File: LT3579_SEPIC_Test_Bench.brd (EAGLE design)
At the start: 64.4 x 62.2 mm, 164 parts

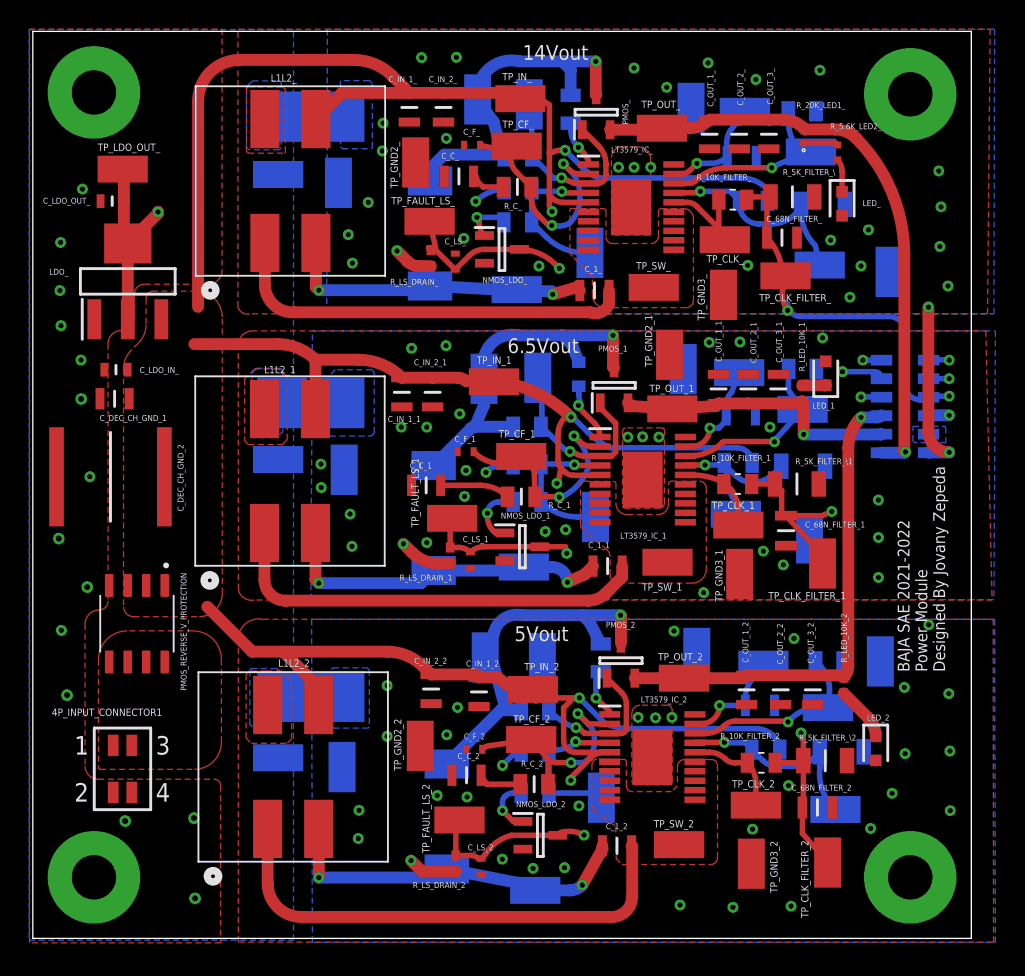
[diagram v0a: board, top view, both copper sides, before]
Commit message: Modified Board Layout
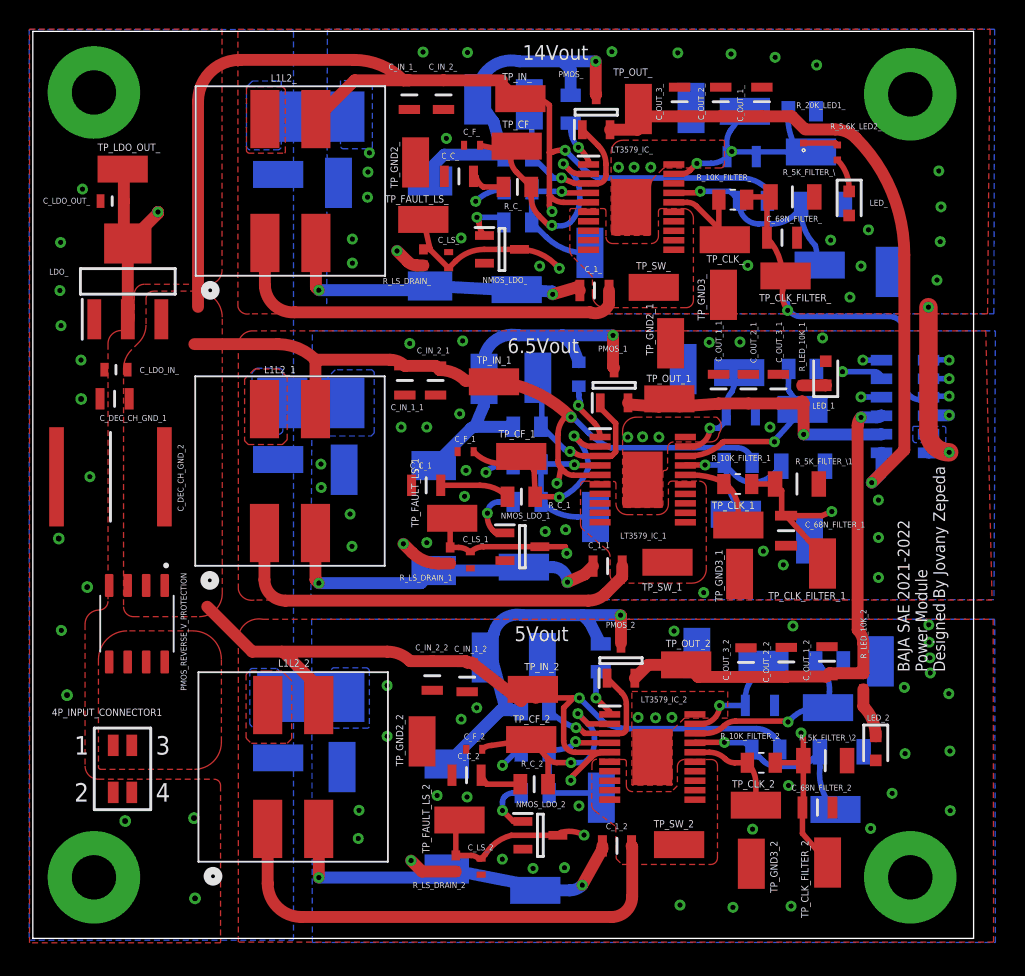
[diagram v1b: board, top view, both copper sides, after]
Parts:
- moved C_OUT_3_ 6.52 mm to (44.4, 57.4), turned to 90 degrees
- moved C_OUT_1_2 5.85 mm to (54.5, 19.0), turned to 90 degrees
- moved C_OUT_3_2 4.96 mm to (48.9, 18.9), turned to 90 degrees
- moved C_OUT_1_ 4.23 mm to (50.0, 57.4), turned to 90 degrees
- moved C_OUT_2_ 2.56 mm to (47.2, 57.4), turned to 90 degrees
- moved TP_OUT_ 2.08 mm to (41.5, 56.9), turned to 270 degrees
- moved C_OUT_2_2 1.95 mm to (51.7, 19.0), turned to 90 degrees
- moved R_LED_10K_2 1.37 mm to (57.0, 17.6)
- moved C_IN_1_2 1.30 mm to (29.8, 17.9)
- moved TP_OUT_2 0.93 mm to (44.8, 18.8)
- moved C_IN_2_2 0.92 mm to (27.4, 18.0)
- moved C_IN_1_ 0.86 mm to (25.8, 57.9)
- moved C_IN_2_ 0.86 mm to (28.2, 57.9)
- moved C_IN_2_1 0.84 mm to (27.6, 38.3)
- moved C_IN_1_1 0.84 mm to (25.5, 38.3)
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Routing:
- net VOUT_: track 41.2 -> 46.4 mm
- net RT_: track 13.7 -> 9.29 mm
- net GND_2: track 16.4 -> 18.7 mm, vias 31 -> 34
- net VOUT_2: track 34.0 -> 35.8 mm
- net LDO_OUT_: track 92.4 -> 91.9 mm
- net VIN: track 207.5 -> 208.0 mm
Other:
- board size 64.4 x 62.2 mm -> 64.5 x 62.2 mm

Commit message: Added more GND Vias, Changes text size, moved texts, clears DRC error
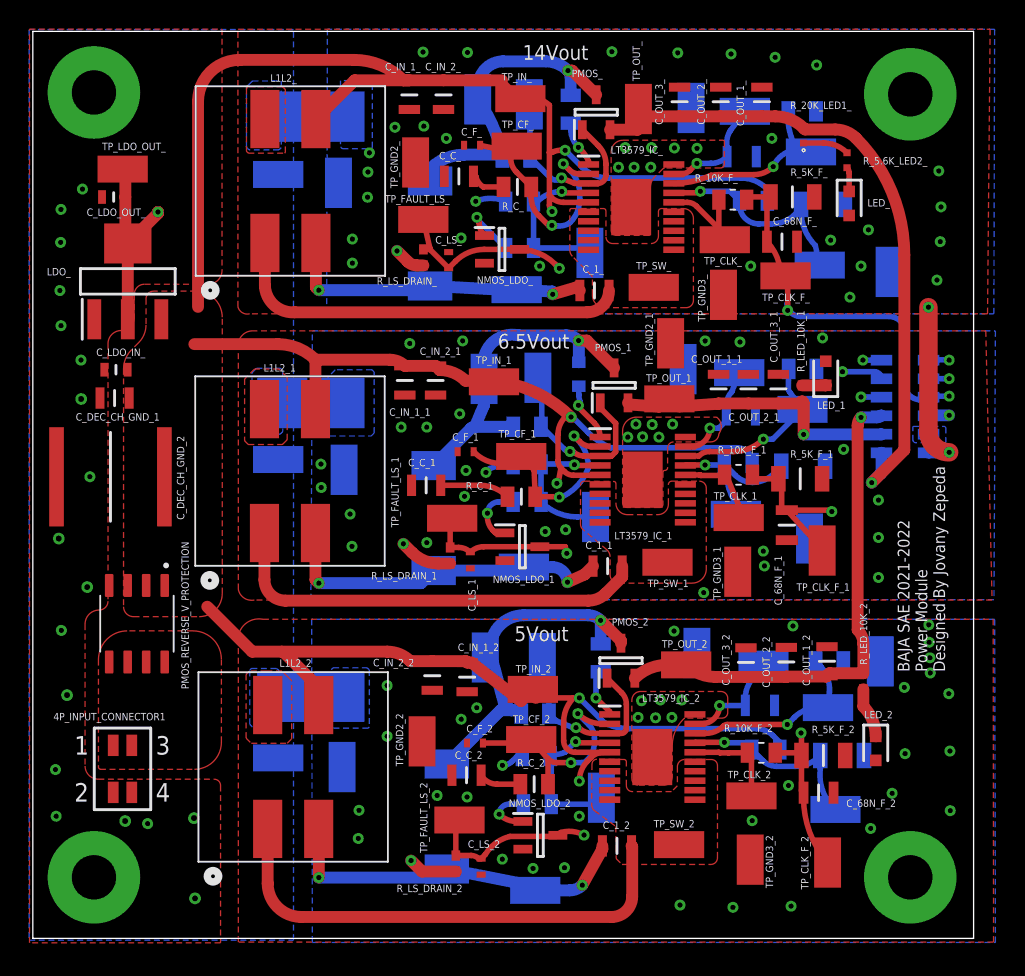
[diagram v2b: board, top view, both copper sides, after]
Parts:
- removed C_68N_FILTER_, C_68N_FILTER_1, C_68N_FILTER_2: CEU4J2X7R1H683K125AE, SamacSys_Parts:CAPC2013X150N
- removed R_10K_FILTER_1, R_10K_FILTER_2: AC0805DR-0710KL, AC0805DR-0710KL:RESC2012X60N
- removed R_5K_FILTER_\1, R_5K_FILTER_\2: RT1206BRD075KL, SamacSys_Parts:RESC3116X65N
- removed TP_CLK_FILTER_1: S1751-46R, S1751-46R:S1751-46R_
- added C_68N_F_, C_68N_F_1, C_68N_F_2: CEU4J2X7R1H683K125AE, SamacSys_Parts:CAPC2013X150N
- added R_10K_F_1, R_10K_F_2: AC0805DR-0710KL, AC0805DR-0710KL:RESC2012X60N
- added R_5K_F_1, R_5K_F_2: RT1206BRD075KL, SamacSys_Parts:RESC3116X65N
- added TP_CLK_F_1: S1751-46R, S1751-46R:S1751-46R_
- moved R_LS_GATE_ 1.76 mm to (33.4, 47.4)
- moved R_5.6K_LED2_ 0.85 mm to (55.9, 53.4)
- moved R_FAULT_ 0.84 mm to (33.4, 50.5)
- moved R_LS_GATE_2 0.78 mm to (34.6, 9.21)
- moved TP_CLK_2 0.70 mm to (49.3, 9.78)
- moved TP_CLK_1 0.51 mm to (48.4, 28.9)
- moved C_F_2 0.43 mm to (30.3, 13.4)
- moved R_FAULT_2 0.31 mm to (34.5, 12.5)
- moved C_LDO_OUT_ 0.30 mm to (5.55, 50.9)
- moved TP_GND3_2 0.29 mm to (49.2, 5.40)
- moved R_UVLO2_2 0.26 mm to (55.5, 12.5)
- moved R_GATE_2 0.23 mm to (34.5, 15.4)
- moved TP_GND3_1 0.20 mm to (48.4, 25.2)
- moved R_GATE_ 0.15 mm to (33.2, 53.6)
- moved C_DEC_CH_GND_1 0.05 mm to (5.61, 37.1)
- renumbered R_10K_FILTER_ to R_10K_F_, R_5K_FILTER_\ to R_5K_F_, TP_CLK_FILTER_ to TP_CLK_F_, TP_CLK_FILTER_2 to TP_CLK_F_2
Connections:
- net CLK_1: now also R_10K_F_1.1; no longer R_10K_FILTER_1.1
- net CLK_2: now also R_10K_F_2.1; no longer R_10K_FILTER_2.1
- net CLK_FILTER_OUT_: now also C_68N_F_.1; no longer C_68N_FILTER_.1
- net CLK_FILTER_OUT_1: now also C_68N_F_1.1, R_10K_F_1.2, R_5K_F_1.1, TP_CLK_F_1.1; no longer C_68N_FILTER_1.1, R_10K_FILTER_1.2, R_5K_FILTER_\1.1, TP_CLK_FILTER_1.1
- net CLK_FILTER_OUT_2: now also C_68N_F_2.1, R_10K_F_2.2, R_5K_F_2.1; no longer C_68N_FILTER_2.1, R_10K_FILTER_2.2, R_5K_FILTER_\2.1
- net GND_: now also C_68N_F_.2; no longer C_68N_FILTER_.2
- net GND_1: now also C_68N_F_1.2, R_5K_F_1.2; no longer C_68N_FILTER_1.2, R_5K_FILTER_\1.2
- net GND_2: now also C_68N_F_2.2, R_5K_F_2.2; no longer C_68N_FILTER_2.2, R_5K_FILTER_\2.2
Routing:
- net RT_: track 9.29 -> 13.8 mm
- net N$13: track 24.9 -> 22.7 mm
- net N$3: track 25.2 -> 23.1 mm
- net N$7: track 26.0 -> 24.3 mm
- net N$8: track 3.35 -> 4.27 mm
- net N$12: track 2.37 -> 3.11 mm
- net N$15: track 2.32 -> 1.66 mm
- net VOUT_2: track 35.8 -> 35.2 mm
- net GND_2: vias 34 -> 37
- net GND_: vias 29 -> 36

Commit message: Used SRC to change the LBR reference of each componant
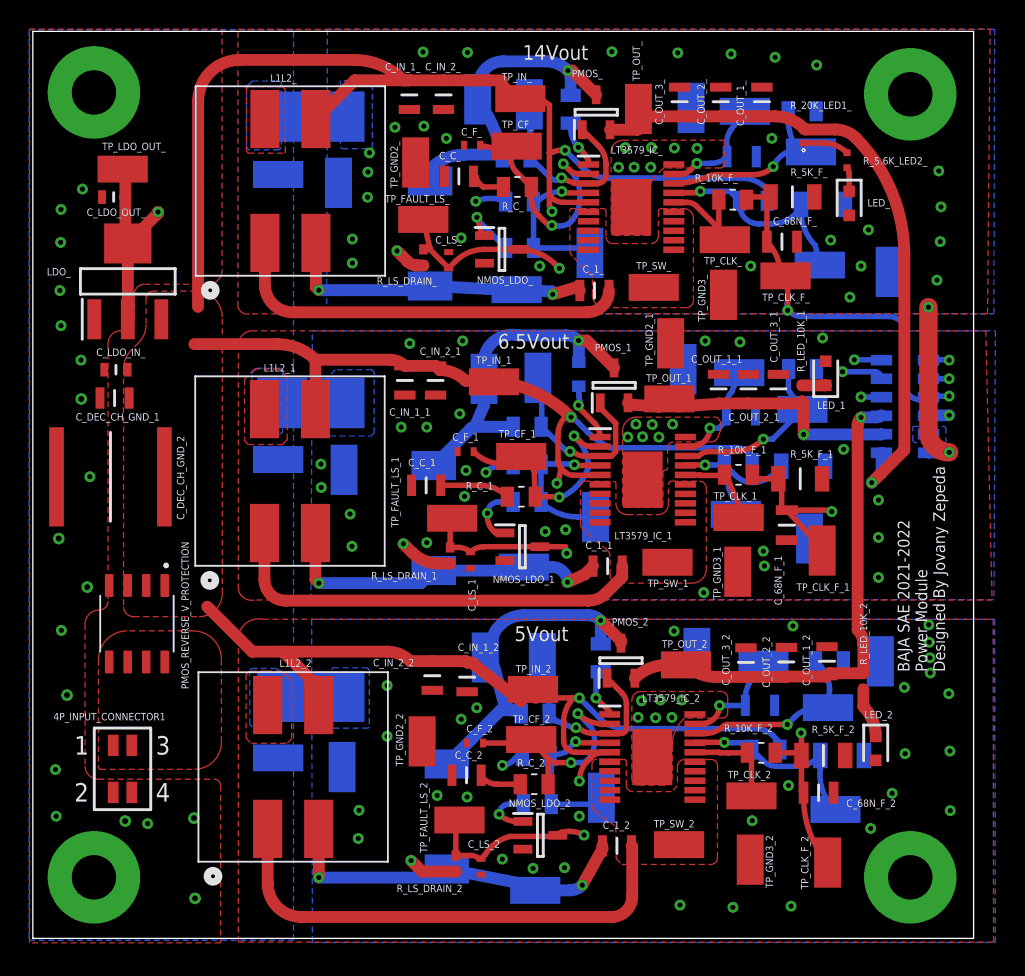
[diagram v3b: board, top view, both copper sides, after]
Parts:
- 12P_OUTPUT_CONNECTOR1: device SamacSys_Parts:CLP-106-02-XXX -> LT3579_SEPIC_Test_Bench:CLP-106-02-XXX
- 4P_INPUT_CONNECTOR1: device SAMTEC-CLP-102-02-X-D:SAMTEC-CLP-102-02-X-D -> LT3579_SEPIC_Test_Bench:SAMTEC-CLP-102-02-X-D
- C_1_, C_1_1, C_1_2, C_IN_1_, C_IN_1_1, C_IN_1_2, C_IN_2_, C_IN_2_1, C_IN_2_2, C_OUT_1_, C_OUT_1_1, C_OUT_1_2, C_OUT_2_, C_OUT_2_1, C_OUT_2_2, C_OUT_3_, C_OUT_3_1, C_OUT_3_2, C_SS_, C_SS_1, C_SS_2: device SamacSys_Parts:CAPC2012X145N -> LT3579_SEPIC_Test_Bench:CAPC2012X145N
- C_68N_F_, C_68N_F_1, C_68N_F_2: device SamacSys_Parts:CAPC2013X150N -> LT3579_SEPIC_Test_Bench:CAPC2013X150N
- C_C_, C_C_1, C_C_2, C_DEC_CH_GND_1: device SamacSys_Parts:CAPC2012X100N -> LT3579_SEPIC_Test_Bench:CAPC2012X100N
- C_DEC_CH_GND_2: device SamacSys_Parts:CAPC7563X250N -> LT3579_SEPIC_Test_Bench:CAPC7563X250N
- C_F_, C_F_1, C_F_2, C_LS_, C_LS_1, C_LS_2: device SamacSys_Parts:CAPC1005X55N -> LT3579_SEPIC_Test_Bench:CAPC1005X55N
- C_LDO_IN_, C_LDO_OUT_: device SamacSys_Parts:CAPC1608X90N -> LT3579_SEPIC_Test_Bench:CAPC1608X90N
- D1_, D1_1, D1_2: device SamacSys_Parts:DIOM7958X256N -> LT3579_SEPIC_Test_Bench:DIOM7958X256N
- L1L2_, L1L2_1, L1L2_2: device MSD1278T-Series:MSD1278T-822MLXX -> LT3579_SEPIC_Test_Bench:MSD1278T-822MLXX
- LDO_: device SamacSys_Parts:SOT230P700X180-4N -> LT3579_SEPIC_Test_Bench:SOT230P700X180-4N
- LED_, LED_1, LED_2: device SamacSys_Parts:APT1608CGCK -> LT3579_SEPIC_Test_Bench:APT1608CGCK
- LT3579_IC_, LT3579_IC_1, LT3579_IC_2: device SamacSys_Parts:SOP65P640X120-21N -> LT3579_SEPIC_Test_Bench:SOP65P640X120-21N
- NMOS_LDO_, NMOS_LDO_1, NMOS_LDO_2, PMOS_, PMOS_1, PMOS_2: device SamacSys_Parts:SOT95P280X100-3N -> LT3579_SEPIC_Test_Bench:SOT95P280X100-3N
- PMOS_REVERSE_V_PROTECTION: device DMP3015LSSQ-13:SOIC127P600X170-8N -> LT3579_SEPIC_Test_Bench:SOIC127P600X170-8N
- R_10K_F_, R_10K_F_1, R_10K_F_2: device AC0805DR-0710KL:RESC2012X60N -> LT3579_SEPIC_Test_Bench:RESC2012X60N
- R_20K_LED1_: device SamacSys_Parts:ERJ2R_(0402) -> LT3579_SEPIC_Test_Bench:ERJ2R_(0402)
- R_5.6K_LED2_: device SamacSys_Parts:ERA2AED122X -> LT3579_SEPIC_Test_Bench:ERA2AED122X
- R_5K_F_, R_5K_F_1, R_5K_F_2, R_UVLO2_, R_UVLO2_1, R_UVLO2_2: device SamacSys_Parts:RESC3116X65N -> LT3579_SEPIC_Test_Bench:RESC3116X65N
- R_C_, R_C_1, R_C_2, R_GATE_, R_GATE_1, R_GATE_2, R_T_, R_T_1, R_T_2: device SamacSys_Parts:RESC2012X60N -> LT3579_SEPIC_Test_Bench:RESC2012X60N
- R_FAULT_, R_FAULT_1, R_FAULT_2, R_LS_GATE_, R_LS_GATE_1, R_LS_GATE_2: device AT0805FRE07100KL:RESC2012X60N -> LT3579_SEPIC_Test_Bench:RESC2012X60N
- R_FB_: device AC0805FR-07150KL:RESC2012X60N -> LT3579_SEPIC_Test_Bench:RESC2012X60N
- R_FB_1: device AC0603FR-0764K9L:RESC1608X55N -> LT3579_SEPIC_Test_Bench:RESC1608X55N
- R_FB_2: device AC0805FR-0745K3L:RESC2012X60N -> LT3579_SEPIC_Test_Bench:RESC2012X60N
- R_LED_10K_1, R_LED_10K_2, R_LS_DRAIN_, R_LS_DRAIN_1, R_LS_DRAIN_2: device SamacSys_Parts:RESC1005X37N -> LT3579_SEPIC_Test_Bench:RESC1005X37N
- R_SHUNT_GND_, R_SHUNT_GND_1, R_SHUNT_GND_2: device GMR100HTCFAR100:RESC6432X55N -> LT3579_SEPIC_Test_Bench:RESC6432X55N
- R_UVLO1_, R_UVLO1_1, R_UVLO1_2: device AC0805FR-0730KL:RESC2012X60N -> LT3579_SEPIC_Test_Bench:RESC2012X60N
- TP_CF_, TP_CF_1, TP_CF_2, TP_CH_GND_, TP_CH_GND_1, TP_CH_GND_2, TP_CLK_, TP_CLK_1, TP_CLK_2, TP_CLK_F_, TP_CLK_F_1, TP_CLK_F_2, TP_D1_, TP_D1_1, TP_D1_2, TP_FAULT_, TP_FAULT_1, TP_FAULT_2, TP_FAULT_LS_, TP_FAULT_LS_1, TP_FAULT_LS_2, TP_FB_, TP_FB_1, TP_FB_2, TP_GATE_, TP_GATE_1, TP_GATE_2, TP_GND1_, TP_GND1_1, TP_GND1_2, TP_GND2_, TP_GND2_1, TP_GND2_2, TP_GND3_, TP_GND3_1, TP_GND3_2, TP_GND4_, TP_GND4_1, TP_GND4_2, TP_GND_, TP_GND_1, TP_GND_2, TP_IN_, TP_IN_1, TP_IN_2, TP_LDO_OUT_, TP_OUT_, TP_OUT_1, TP_OUT_2, TP_RT_, TP_RT_1, TP_RT_2, TP_SHDN_, TP_SHDN_1, TP_SHDN_2, TP_SS_, TP_SS_1, TP_SS_2, TP_SW_, TP_SW_1, TP_SW_2: device S1751-46R:S1751-46R_ -> LT3579_SEPIC_Test_Bench:S1751-46R_
- U$1, U$2, U$3, U$4: device THROUGH_HOLE:THROUGH_HOLE -> LT3579_SEPIC_Test_Bench:THROUGH_HOLE

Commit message: Modifed board. Connected GND planes Together.
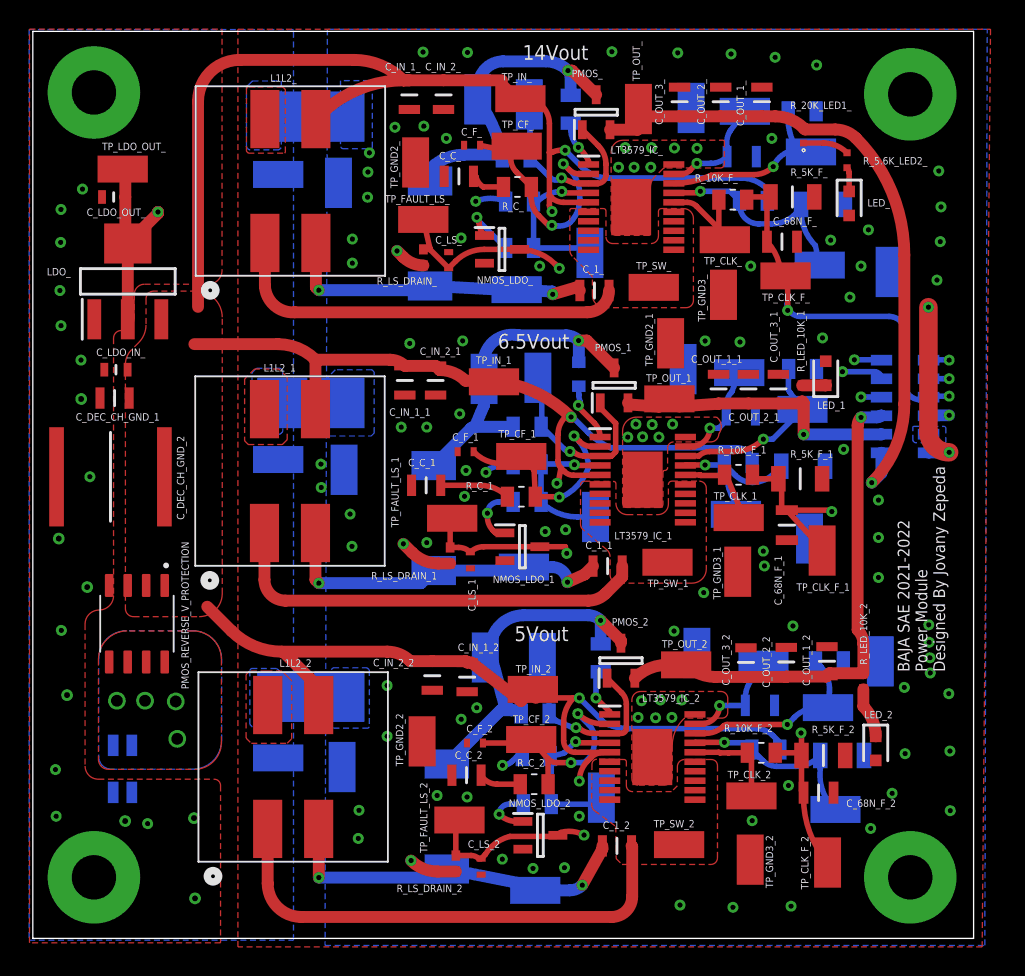
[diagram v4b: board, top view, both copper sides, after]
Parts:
- flipped 4P_INPUT_CONNECTOR1 to the bottom
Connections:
- removed net GND_: 12P_OUTPUT_CONNECTOR1.12, C_68N_F_.2, C_C_.2, C_F_.2, C_IN_1_.2, C_IN_2_.2, C_LS_.2, C_OUT_1_.2, C_OUT_2_.2, C_OUT_3_.2, C_SS_.2, L1L2_.4, LED_.2, LT3579_IC_.20, LT3579_IC_.21, NMOS_LDO_.2, R_5K_F_.2, R_SHUNT_GND_.2, R_T_.2, R_UVLO2_.1, TP_GND1_.1, TP_GND2_.1, TP_GND3_.1, TP_GND4_.1, TP_GND_.1
- removed net GND_1: 12P_OUTPUT_CONNECTOR1.10, C_68N_F_1.2, C_C_1.2, C_F_1.2, C_IN_1_1.2, C_IN_2_1.2, C_LS_1.2, C_OUT_1_1.2, C_OUT_2_1.2, C_OUT_3_1.2, C_SS_1.2, L1L2_1.4, LED_1.2, LT3579_IC_1.20, LT3579_IC_1.21, NMOS_LDO_1.2, R_5K_F_1.2, R_SHUNT_GND_1.2, R_T_1.2, R_UVLO2_1.1, TP_GND1_1.1, TP_GND2_1.1, TP_GND3_1.1, TP_GND4_1.1, TP_GND_1.1
- removed net GND_2: 12P_OUTPUT_CONNECTOR1.8, C_68N_F_2.2, C_C_2.2, C_F_2.2, C_IN_1_2.2, C_IN_2_2.2, C_LS_2.2, C_OUT_1_2.2, C_OUT_2_2.2, C_OUT_3_2.2, C_SS_2.2, L1L2_2.4, LED_2.2, LT3579_IC_2.20, LT3579_IC_2.21, NMOS_LDO_2.2, R_5K_F_2.2, R_SHUNT_GND_2.2, R_T_2.2, R_UVLO2_2.1, TP_GND1_2.1, TP_GND2_2.1, TP_GND3_2.1, TP_GND4_2.1, TP_GND_2.1
- new net GND: 12P_OUTPUT_CONNECTOR1.10, 12P_OUTPUT_CONNECTOR1.12, 12P_OUTPUT_CONNECTOR1.8, C_68N_F_.2, C_68N_F_1.2, C_68N_F_2.2, C_C_.2, C_C_1.2, C_C_2.2, C_F_.2, C_F_1.2, C_F_2.2, C_IN_1_.2, C_IN_1_1.2, C_IN_1_2.2, C_IN_2_.2, C_IN_2_1.2, C_IN_2_2.2, C_LS_.2, C_LS_1.2, C_LS_2.2, C_OUT_1_.2, C_OUT_1_1.2, C_OUT_1_2.2, C_OUT_2_.2, C_OUT_2_1.2, C_OUT_2_2.2, C_OUT_3_.2, C_OUT_3_1.2, C_OUT_3_2.2, C_SS_.2, C_SS_1.2, C_SS_2.2, L1L2_.4, L1L2_1.4, L1L2_2.4, LED_.2, LED_1.2, LED_2.2, LT3579_IC_.20, LT3579_IC_.21, LT3579_IC_1.20, LT3579_IC_1.21, LT3579_IC_2.20, LT3579_IC_2.21, NMOS_LDO_.2, NMOS_LDO_1.2, NMOS_LDO_2.2, R_5K_F_.2, R_5K_F_1.2, R_5K_F_2.2, R_SHUNT_GND_.2, R_SHUNT_GND_1.2, R_SHUNT_GND_2.2, R_T_.2, R_T_1.2, R_T_2.2, R_UVLO2_.1, R_UVLO2_1.1, R_UVLO2_2.1, TP_GND1_.1, TP_GND1_1.1, TP_GND1_2.1, TP_GND2_.1, TP_GND2_1.1, TP_GND2_2.1, TP_GND3_.1, TP_GND3_1.1, TP_GND3_2.1, TP_GND4_.1, TP_GND4_1.1, TP_GND4_2.1, TP_GND_.1, TP_GND_1.1, TP_GND_2.1
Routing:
- net GND: track 0.00 -> 30.7 mm, vias 0 -> 103
- net GND_2: track 18.7 -> 0.00 mm, vias 37 -> 0
- net GND_: track 12.0 -> 0.00 mm, vias 36 -> 0
- net VIN: track 208.1 -> 206.6 mm
- added copper zone on layer 1, net GND
- added copper zone on layer 16, net GND
- added copper zone on layer 16, net VIN_CONNECTOR
- removed copper zone on layer 1, net GND_
- removed copper zone on layer 16, net GND_
- removed copper zone on layer 1, net GND_1
- removed copper zone on layer 16, net GND_1
- removed copper zone on layer 1, net GND_2
- removed copper zone on layer 16, net GND_2
